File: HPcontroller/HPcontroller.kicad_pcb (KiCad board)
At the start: 2 copper layers, 100 x 62 mm, 38 parts, among them Q1 Q_Dual_NMOS_S1G1S2G2D2D2D1D1, SW1 SW_SPDT, SW2 SW_SPST, SW3 SW_SPST, SW4 SW_SPST, SW5 SW_SPST, U1 Adafruit_QTPY_ESP32-C3, U2 NCP81071B, U3 MIC841N, U4 VR10S3V3, U5 ER-OLED0.49-1_MODULE, U6 Adafruit_MAX31850

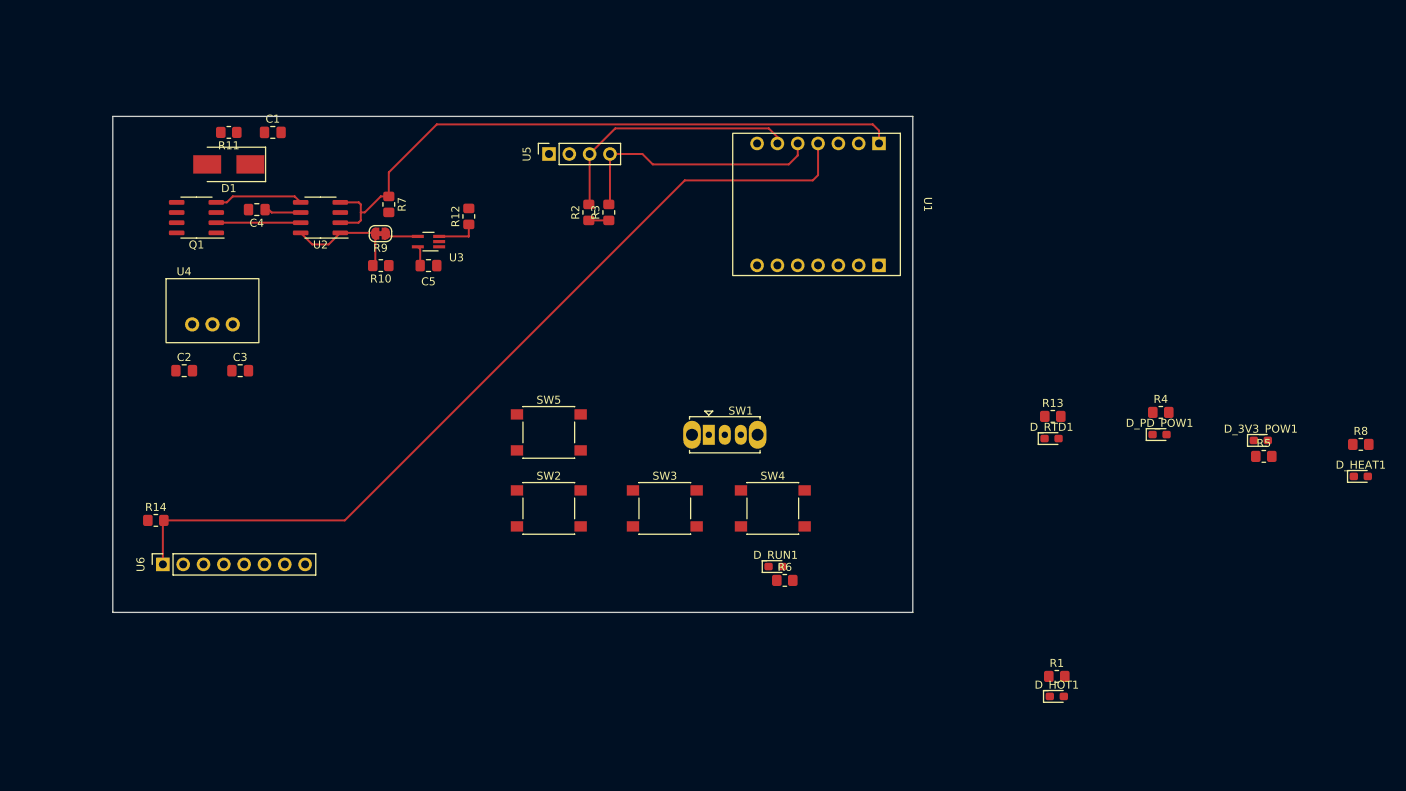
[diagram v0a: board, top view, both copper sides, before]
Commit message: routing more.  waitingfor PD trigger to arrive
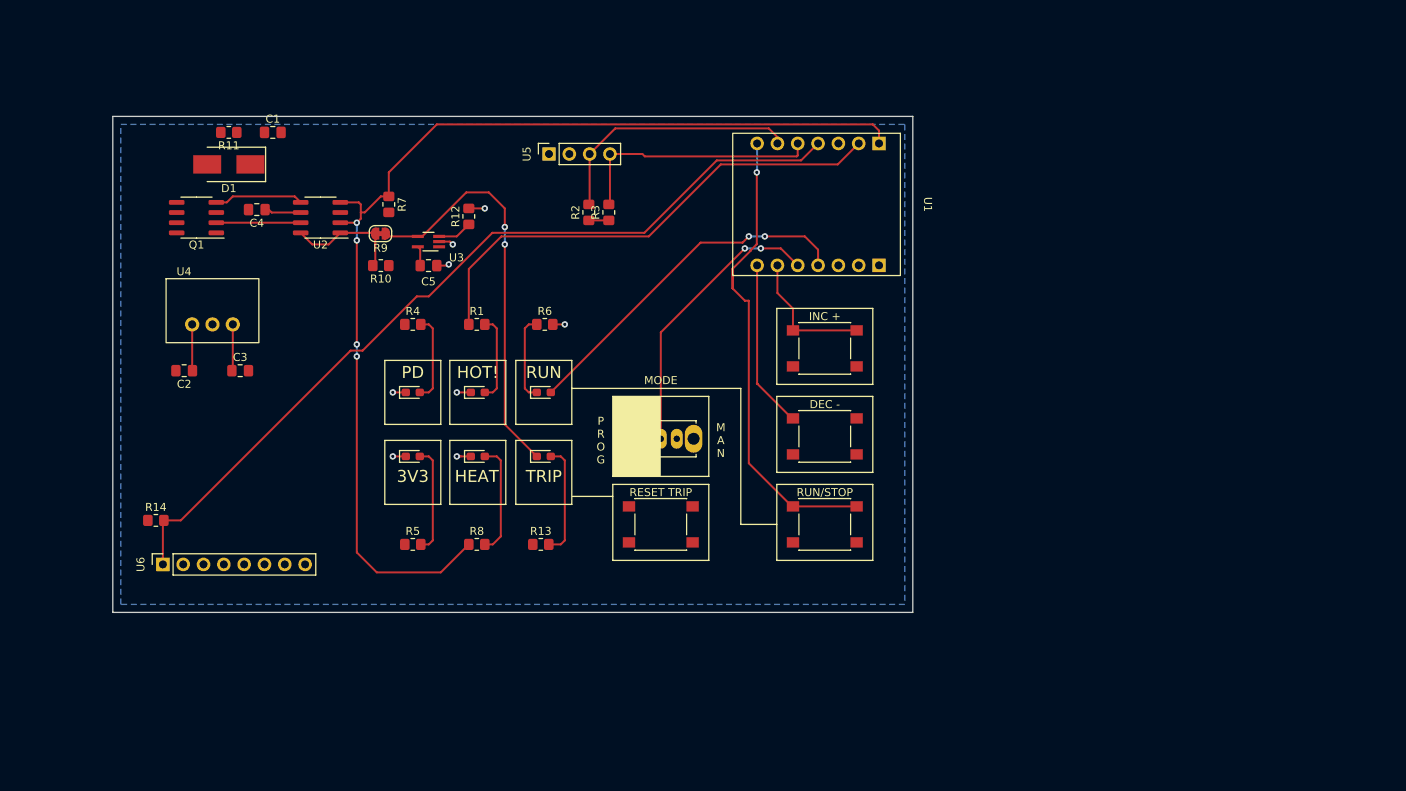
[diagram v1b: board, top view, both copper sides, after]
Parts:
- moved R8 111.2 mm to (118.5, 103.0)
- moved D_HEAT1 110.4 mm to (118.6, 92.0)
- moved R5 106.9 mm to (110.5, 103.0)
- moved D_3V3_POW1 106.0 mm to (110.5, 92.0)
- moved R4 94.1 mm to (110.5, 75.5)
- moved D_PD_POW1 93.5 mm to (110.5, 84.0)
- moved R1 84.8 mm to (118.5, 75.5)
- moved D_HOT 81.7 mm to (118.6, 84.0)
- moved R13 66.0 mm to (126.5, 103.0)
- moved D_RTD1 63.5 mm to (126.9, 92.0)
- moved R6 43.9 mm to (127.0, 75.5)
- moved SWINC1 39.9 mm to (162.0, 78.5)
- moved D_RUN1 36.2 mm to (126.9, 84.0)
- moved SWDEC1 21.9 mm to (162.0, 89.5)
- moved SWRST1 18.1 mm to (141.5, 100.5)
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- renumbered D_HOT1 to D_HOT, SW3 to SWDEC1, SW2 to SWINC1, SW1 to SWMODE1, SW5 to SWRST1, SW4 to SWRUN1
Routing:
- net Net-(R1-Pad1): track 0.00 -> 62.2 mm
- net /RUN: track 0.00 -> 60.6 mm, vias 0 -> 1
- net /FET_DRIVE: track 80.4 -> 137.9 mm, vias 0 -> 4
- net /ThermalProtector/THM_PROT_OUT: track 4.16 -> 50.8 mm, vias 0 -> 2
- net Net-(D_RUN1-Pad2): track 0.00 -> 44.1 mm, vias 0 -> 2
- net /MODE: track 0.00 -> 35.6 mm, vias 0 -> 2
- net /DEC: track 0.00 -> 21.2 mm
- net /INC: track 0.00 -> 16.9 mm
- net Net-(D_RTD1-Pad2): track 0.00 -> 14.2 mm
- net Net-(D_HEAT1-Pad2): track 0.00 -> 14.1 mm
- net GND: track 0.00 -> 13.7 mm, vias 0 -> 8
- net Net-(D_3V3_POW1-Pad2): track 0.00 -> 13.5 mm
- net Net-(D_PD_POW1-Pad2): track 0.00 -> 11.0 mm
- net Net-(D_RUN1-Pad1): track 0.00 -> 10.9 mm
- net Net-(D_HOT1-Pad2): track 0.00 -> 10.9 mm
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- added copper zone on B.Cu, net GND
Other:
- board text added: "3V3"
- board text added: "DEC -"
- board text added: "HEAT"
- board text added: "HOT!"
- board text added: "INC +"
- board text added: "M A N"
- board text added: "MODE"
- board text added: "P R O G"
- board text added: "PD"
- board text added: "RESET TRIP"
- board text added: "RUN"
- board text added: "RUN/STOP"
- board text added: "TRIP"

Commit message: minor pcb change to give TC wires more room
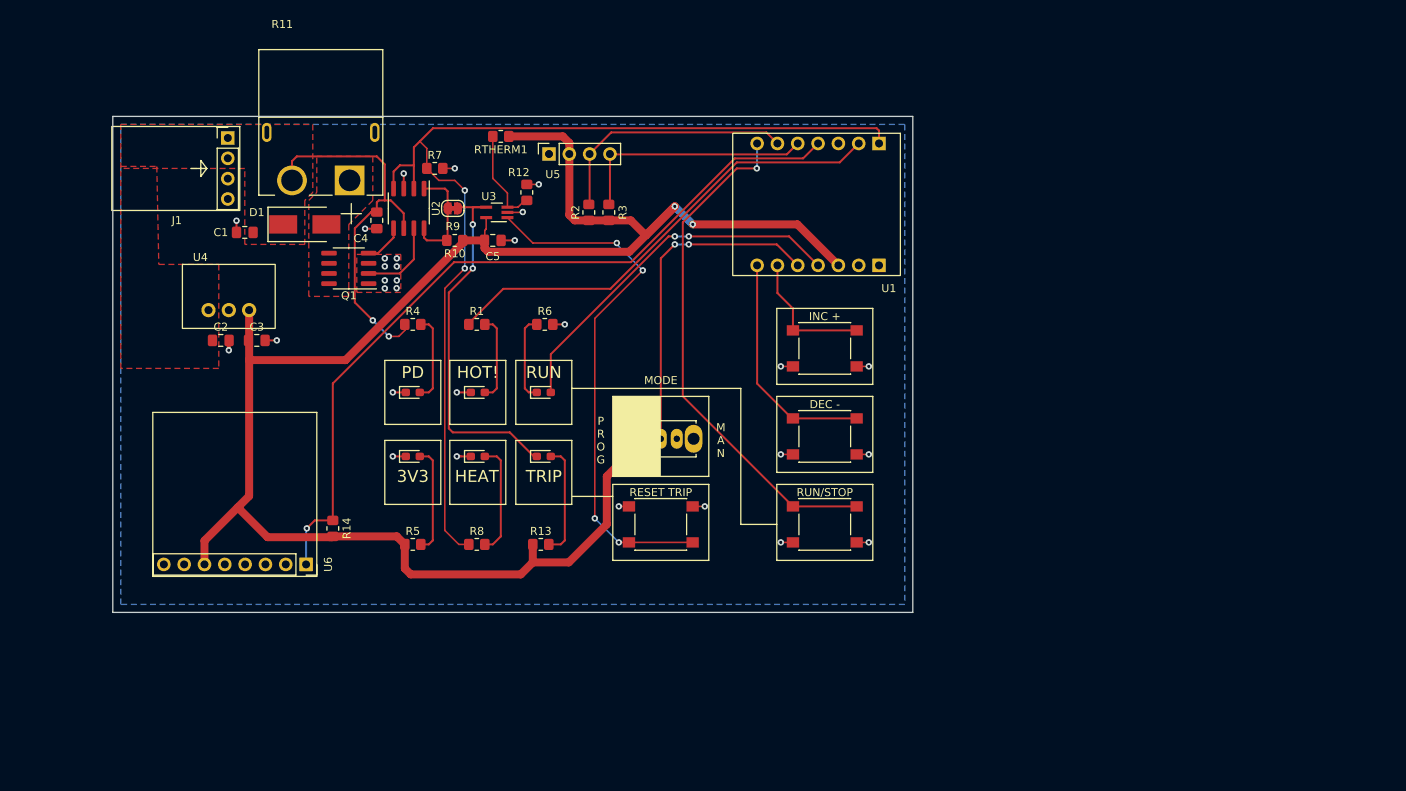
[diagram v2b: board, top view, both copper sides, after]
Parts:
- added J1: Screw_Terminal_01x02, connector_custom:PD_trigger, F.Cu at (87.4, 56.0)
- added RTHERM1: 10kTHERM, Resistor_SMD:R_0805_2012Metric_Pad1.20x1.40mm_HandSolder, F.Cu at (121.5, 52.0)
- R11: footprint Resistor_SMD:R_0805_2012Metric_Pad1.20x1.40mm_HandSolder -> connector_custom:AMASS_XT60PW-M
- moved R14 22.1 mm to (100.5, 101.0), turned to 90 degrees
- moved Q1 20.1 mm to (102.5, 68.5)
- moved U6 17.9 mm to (97.2, 105.5), turned to -90 degrees
- moved C4 15.1 mm to (106.0, 62.5), turned to -90 degrees
- moved C1 13.0 mm to (89.5, 64.0), turned to 180 degrees
- moved D1 12.1 mm to (97.0, 63.0), turned to 0 degrees
- moved R11 11.5 mm to (99.0, 51.5), turned to 0 degrees
- moved U2 11.1 mm to (110.0, 61.0), turned to -90 degrees
- moved R10 9.77 mm to (115.8, 65.0)
- moved R9 9.57 mm to (115.5, 61.0)
- moved U3 9.29 mm to (121.0, 61.5)
- moved C5 8.64 mm to (120.5, 65.0)
- moved R12 7.85 mm to (124.8, 59.0)
- moved R7 7.30 mm to (113.2, 56.0), turned to 0 degrees
- moved C2 5.94 mm to (86.5, 77.5), turned to 0 degrees
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- renumbered D_HOT to D_HOT1
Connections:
- R11 pad 1: VCC -> Net-(D1-Pad2)
- R11 pad 2: Net-(D1-Pad2) -> VCC
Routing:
- net +3V3: track 10.8 -> 226.6 mm, vias 0 -> 2
- net /ThermalProtector/THM_PROT_RES: track 0.00 -> 66.7 mm, vias 0 -> 4
- net VCC: track 9.94 -> 48.3 mm, vias 0 -> 2
- net GND: track 13.7 -> 34.6 mm, vias 8 -> 30
- net /FET_DRIVE: track 137.9 -> 127.9 mm, vias 4 -> 2
- net /OW_DATA: track 106.8 -> 98.4 mm, vias 0 -> 1
- net /DEC: track 21.2 -> 29.5 mm
- net Net-(R12-Pad1): track 4.33 -> 12.4 mm
- net /OUTB: track 11.2 -> 5.10 mm
- net /MODE: track 35.6 -> 41.5 mm
- net /ThermalProtector/THM_PROT_OUT: track 50.8 -> 46.6 mm
- net Net-(R1-Pad1): track 62.2 -> 58.2 mm
- net /RUN: track 60.6 -> 64.3 mm
- net Net-(D_RUN1-Pad2): track 44.1 -> 45.8 mm
- net /SDA: track 31.5 -> 30.4 mm
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- added copper zone on F.Cu, net GND
- added copper zone on F.Cu, net Net-(D1-Pad2)
- added copper zone on F.Cu, net VCC

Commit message: started heater layout.  need to make heater smaller to accomodate some kind of mounting holes, need to add mounting for controller
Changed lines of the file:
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@@
     )
     (pad_to_mask_clearance 0)
+    (grid_origin 73 49.5)
     (pcbplotparams
       (layerselection 0x00010fc_ffffffff)
@@
     (property "Sheetname" "")
     (attr through_hole)
-    (fp_text reference "R11" (at -4.8236 -13.51498) (layer "F.SilkS")
+    (fp_text reference "R11" (at 10 0) (layer "F.SilkS")
       (effects (font (size 1.000441 1.000441) (thickness 0.15)))
     )
@@
     (effects (font (size 1.5 1.5) (thickness 0.3)))
   )
+  (dimension (type orthogonal) (layer "F.Cu")
+    (pts (xy 73 49.5) (xy 91.253 49.595))
+    (height -8.5)
+    (orientation 0)
+    (gr_text "18.2530 mm" (at 82.1265 39.2) (layer "F.Cu")
+      (effects (font (size 1.5 1.5) (thickness 0.3)))
+    )
+    (format (units 3) (units_format 1) (precision 4))
+    (style (thickness 0.2) (arrow_length 1.27) (text_position_mode 0) (extension_height 0.58642) (extension_offset 0.5) keep_text_aligned)
+  )
   (segment (start 106 61.4625) (end 105.2875 61.4625) (width 0.25) (layer "F.Cu") (net 1))

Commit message: fixed minor issues, added mounting
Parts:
- added H1: MountingHole, MountingHole:MountingHole_3.2mm_M3_ISO14580, F.Cu at (76.5, 108.0)
- added H2: MountingHole, MountingHole:MountingHole_3.2mm_M3_ISO14580, F.Cu at (76.5, 53.0)
- added H3: MountingHole, MountingHole:MountingHole_3.2mm_M3_ISO14580, F.Cu at (169.5, 108.0)
- added H4: MountingHole, MountingHole:MountingHole_3.2mm_M3_ISO14580, F.Cu at (169.5, 60.5)
- moved J1 6.71 mm to (84.4, 62.0)
- moved U6 3.00 mm to (97.2, 102.5)
- moved C1 1.80 mm to (90.5, 65.5), turned to -90 degrees
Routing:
- net +3V3: track 226.6 -> 231.7 mm
- net /OW_DATA: track 98.4 -> 96.0 mm

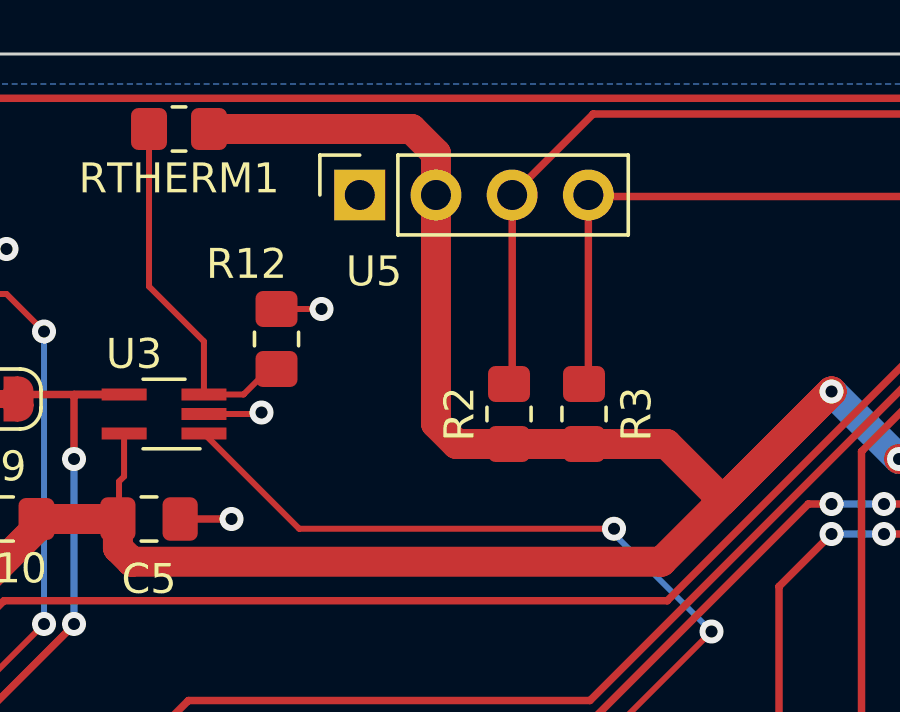
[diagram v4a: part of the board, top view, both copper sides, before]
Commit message: added upllup to thermal protection circuit
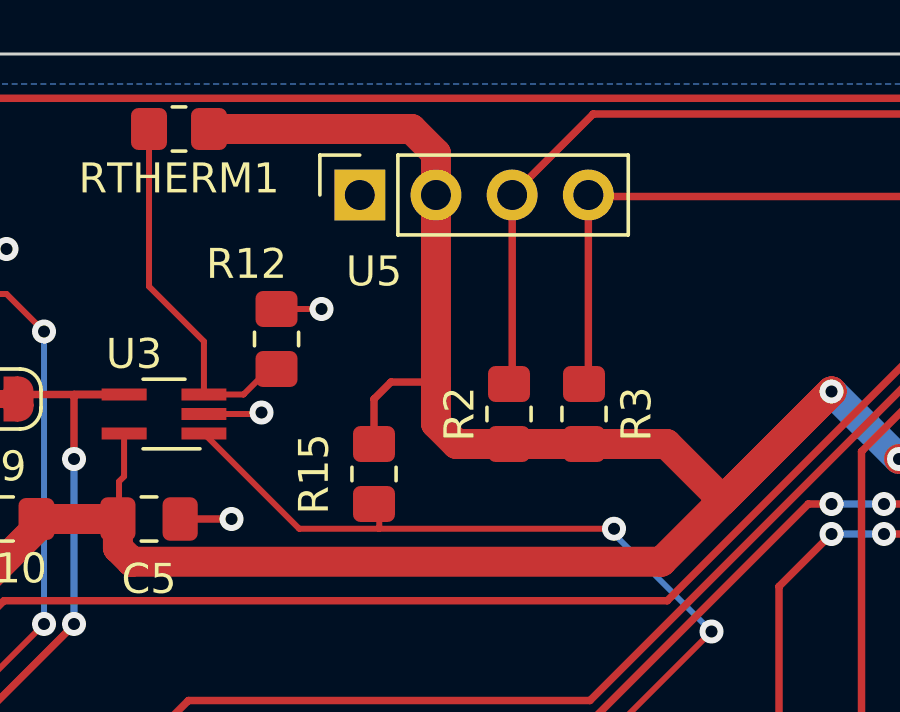
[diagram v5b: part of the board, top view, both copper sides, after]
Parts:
- added R15: 10k, Resistor_SMD:R_0805_2012Metric_Pad1.20x1.40mm_HandSolder, F.Cu at (128.0, 63.5)
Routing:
- net +3V3: track 231.7 -> 235.5 mm
- net /ThermalProtector/THM_PROT_RES: track 66.7 -> 67.6 mm
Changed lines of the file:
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@@
+    )
+  )
+  (footprint "Resistor_SMD:R_0805_2012Metric_Pad1.20x1.40mm_HandSolder" (layer "F.Cu")
+    (at 128 63.5 -90)
+    (descr "Resistor SMD 0805 (2012 Metric), square (rectangular) end terminal, IPC_7351 nominal with elongated pad for handsoldering. (Body size source: IPC-SM-782 page 72, https://www.pcb-3d.com/wordpress/wp-content/uploads/ipc-sm-782a_amendment_1_and_2.pdf), generated with kicad-footprint-generator")
+    (tags "resistor handsolder")
+    (property "Sheetfile" "ThermalProtector.kicad_sch")
+    (property "Sheetname" "ThermalProtector")
+    (attr smd)
+    (fp_text reference "R15" (at 0 2 90) (layer "F.SilkS")
+      (effects (font (size 1 1) (thickness 0.15)))
+    )
+    (fp_text value "10k" (at 0 1.65 90) (layer "F.Fab")
+      (effects (font (size 1 1) (thickness 0.15)))
+    )
+    (fp_text user "${REFERENCE}" (at 0 0 90) (layer "F.Fab")
+      (effects (font (size 0.5 0.5) (thickness 0.08)))
+    )
+    (fp_line (start -0.227064 -0.735) (end 0.227064 -0.735) (layer "F.SilkS") (width 0.12))
+    (fp_line (start -0.227064 0.735) (end 0.227064 0.735) (layer "F.SilkS") (width 0.12))
+    (fp_line (start -1.85 -0.95) (end 1.85 -0.95) (layer "F.CrtYd") (width 0.05))
+    (fp_line (start 1.85 0.95) (end -1.85 0.95) (layer "F.CrtYd") (width 0.05))
+    (fp_line (start -1.85 0.95) (end -1.85 -0.95) (layer "F.CrtYd") (width 0.05))
+    (fp_line (start 1.85 -0.95) (end 1.85 0.95) (layer "F.CrtYd") (width 0.05))
+    (fp_line (start 1 -0.625) (end 1 0.625) (layer "F.Fab") (width 0.1))
+    (fp_line (start 1 0.625) (end -1 0.625) (layer "F.Fab") (width 0.1))
+    (fp_line (start -1 -0.625) (end 1 -0.625) (layer "F.Fab") (width 0.1))
+    (fp_line (start -1 0.625) (end -1 -0.625) (layer "F.Fab") (width 0.1))
+    (pad "1" smd roundrect (at -1 0 270) (size 1.2 1.4) (layers "F.Cu" "F.Paste" "F.Mask") (roundrect_rratio 0.208333)
+      (net 3 "+3V3") (pintype "passive"))
+    (pad "2" smd roundrect (at 1 0 270) (size 1.2 1.4) (layers "F.Cu" "F.Paste" "F.Mask") (roundrect_rratio 0.208333)
+      (net 26 "/ThermalProtector/THM_PROT_RES") (pintype "passive"))
+    (model "${KICAD6_3DMODEL_DIR}/Resistor_SMD.3dshapes/R_0805_2012Metric.wrl"
+      (offset (xyz 0 0 0))
+      (scale (xyz 1 1 1))
+      (rotate (xyz 0 0 0))
     )
   )
@@
   (via (at 108 92) (size 0.8) (drill 0.4) (layers "F.Cu" "B.Cu") (net 2))
   (via (at 107 68.25) (size 0.8) (drill 0.4) (layers "F.Cu" "B.Cu") (free) (net 2))
+  (segment (start 128 62.5) (end 128 61) (width 0.25) (layer "F.Cu") (net 3))
   (segment (start 143.25 60.75) (end 143.25 60.750002) (width 1) (layer "F.Cu") (net 3))
-  (segment (start 130.065 54.2) (end 130.065 61.815) (width 1) (layer "F.Cu") (net 3))
   (segment (start 90 97) (end 84.46 102.54) (width 1) (layer "F.Cu") (net 3))
   (segment (start 109.5 103) (end 109.5 106) (width 1) (layer "F.Cu") (net 3))
@@
   (segment (start 119.5 63.75) (end 119.5 64.9625) (width 0.2) (layer "F.Cu") (net 3))
   (segment (start 130.065 61.815) (end 130.75 62.5) (width 1) (layer "F.Cu") (net 3))
+  (segment (start 130.065 54.2) (end 130.065 60.435) (width 1) (layer "F.Cu") (net 3))
   (segment (start 100 105.5) (end 100.5 105) (width 1) (layer "F.Cu") (net 3))
   (segment (start 134.75 94.5) (end 136.25 93) (width 1) (layer "F.Cu") (net 3))
@@
   (segment (start 116.75 65) (end 119.4625 65) (width 1) (layer "F.Cu") (net 3))
   (segment (start 84.46 102.5) (end 84.46 104.46) (width 1) (layer "F.Cu") (net 3))
+  (segment (start 128 61) (end 128.565 60.435) (width 0.25) (layer "F.Cu") (net 3))
   (segment (start 119.4625 65.9625) (end 119.92452 66.42452) (width 1) (layer "F.Cu") (net 3))
   (segment (start 90.04 79.9625) (end 102.09243 79.9625) (width 1) (layer "F.Cu") (net 3))
@@
   (segment (start 139.625 64.375) (end 143.25 60.75) (width 1) (layer "F.Cu") (net 3))
   (segment (start 137.75 62.5) (end 139.625 64.375) (width 1) (layer "F.Cu") (net 3))
+  (segment (start 128.565 60.435) (end 130.065 60.435) (width 0.25) (layer "F.Cu") (net 3))
   (segment (start 108.5 102) (end 109.5 103) (width 1) (layer "F.Cu") (net 3))
   (segment (start 102.09243 79.9625) (end 116.75 65.30493) (width 1) (layer "F.Cu") (net 3))
   (segment (start 129.25 52) (end 130.065 52.815) (width 1) (layer "F.Cu") (net 3))
   (segment (start 130.75 62.5) (end 132.5 62.5) (width 1) (layer "F.Cu") (net 3))
+  (segment (start 130.065 60.435) (end 130.065 61.815) (width 1) (layer "F.Cu") (net 3))
   (via (at 143.25 60.750002) (size 0.8) (drill 0.4) (layers "F.Cu" "B.Cu") (net 3))
   (via (at 145.5 63) (size 0.8) (drill 0.4) (layers "F.Cu" "B.Cu") (net 3))
@@
   (segment (start 153.538 55.962) (end 153.5 56) (width 0.25) (layer "B.Cu") (net 25))
   (segment (start 137.52 102.75) (end 136.25 102.75) (width 0.2) (layer "F.Cu") (net 26))
+  (segment (start 128.17498 65.32502) (end 128.17498 64.67498) (width 0.2) (layer "F.Cu") (net 26))
   (segment (start 137.52 102.75) (end 145.48 102.75) (width 0.2) (layer "F.Cu") (net 26))
+  (segment (start 128.17498 64.67498) (end 128 64.5) (width 0.2) (layer "F.Cu") (net 26))
   (segment (start 122.33 62.15) (end 125.50502 65.32502) (width 0.2) (layer "F.Cu") (net 26))
+  (segment (start 125.50502 65.32502) (end 128.17498 65.32502) (width 0.2) (layer "F.Cu") (net 26))
   (segment (start 139.25 68.75) (end 133.25 74.75) (width 0.2) (layer "F.Cu") (net 26))
+  (segment (start 128.17498 65.32502) (end 136 65.32502) (width 0.2) (layer "F.Cu") (net 26))
   (segment (start 133.25 74.75) (end 133.25 99.75) (width 0.2) (layer "F.Cu") (net 26))
-  (segment (start 125.50502 65.32502) (end 136 65.32502) (width 0.2) (layer "F.Cu") (net 26))
   (via (at 136 65.32502) (size 0.8) (drill 0.4) (layers "F.Cu" "B.Cu") (net 26))
   (via (at 136.25 102.75) (size 0.8) (drill 0.4) (layers "F.Cu" "B.Cu") (net 26))
